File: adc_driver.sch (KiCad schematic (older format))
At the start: 26 parts, among them U17 DG412xUE, U18 AD8421ARZ, U19 ADA4932-1YCPZ-R7

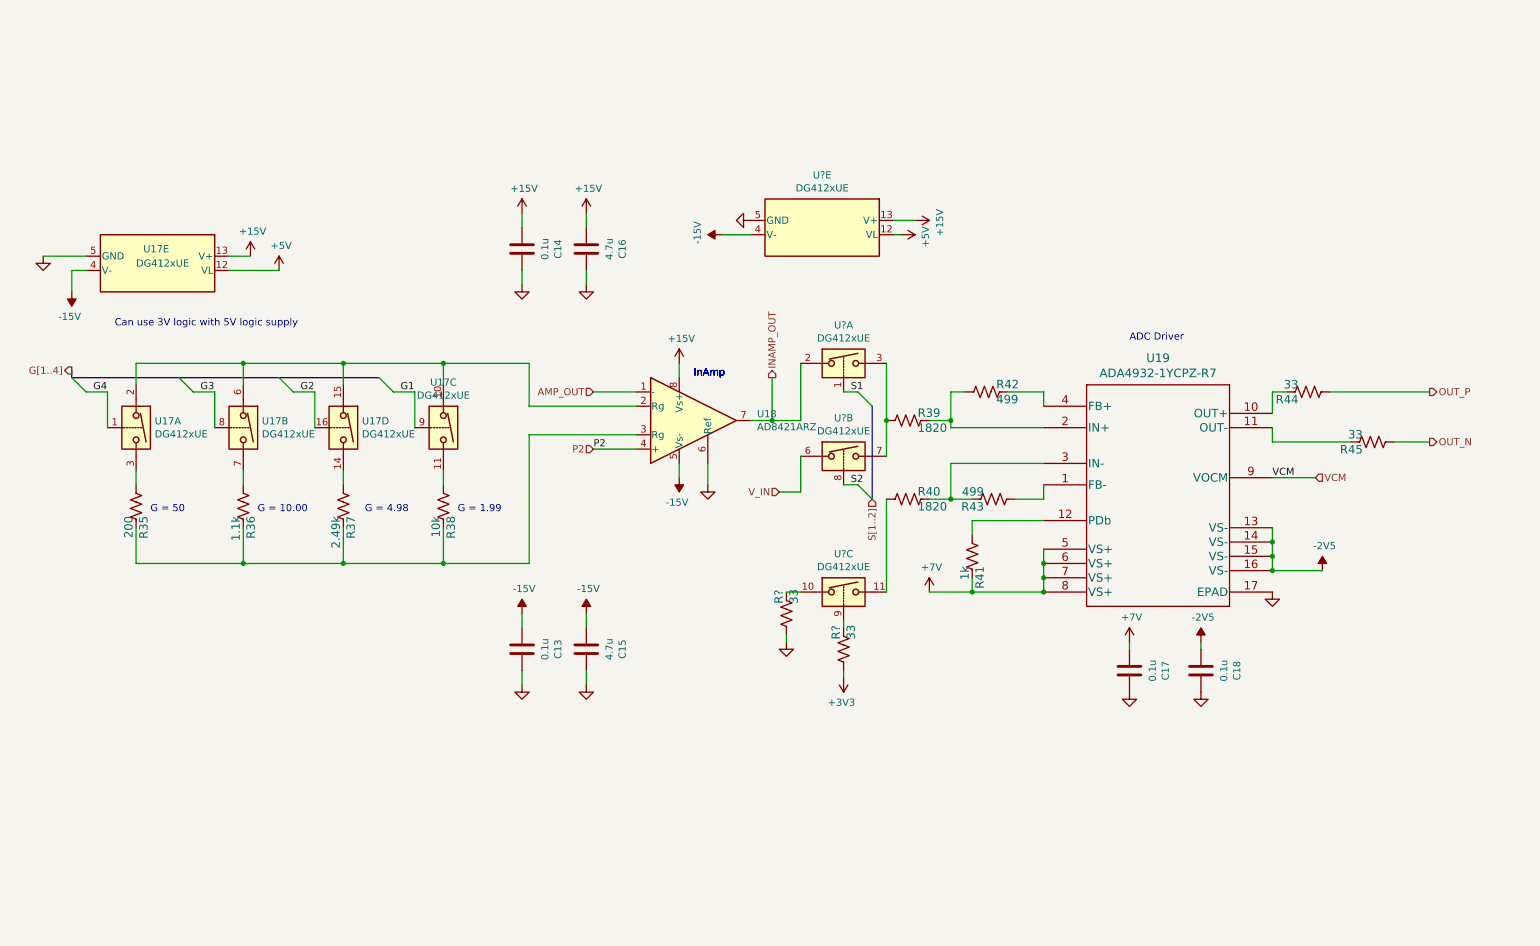
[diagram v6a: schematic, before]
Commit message: update MUX for adc driver
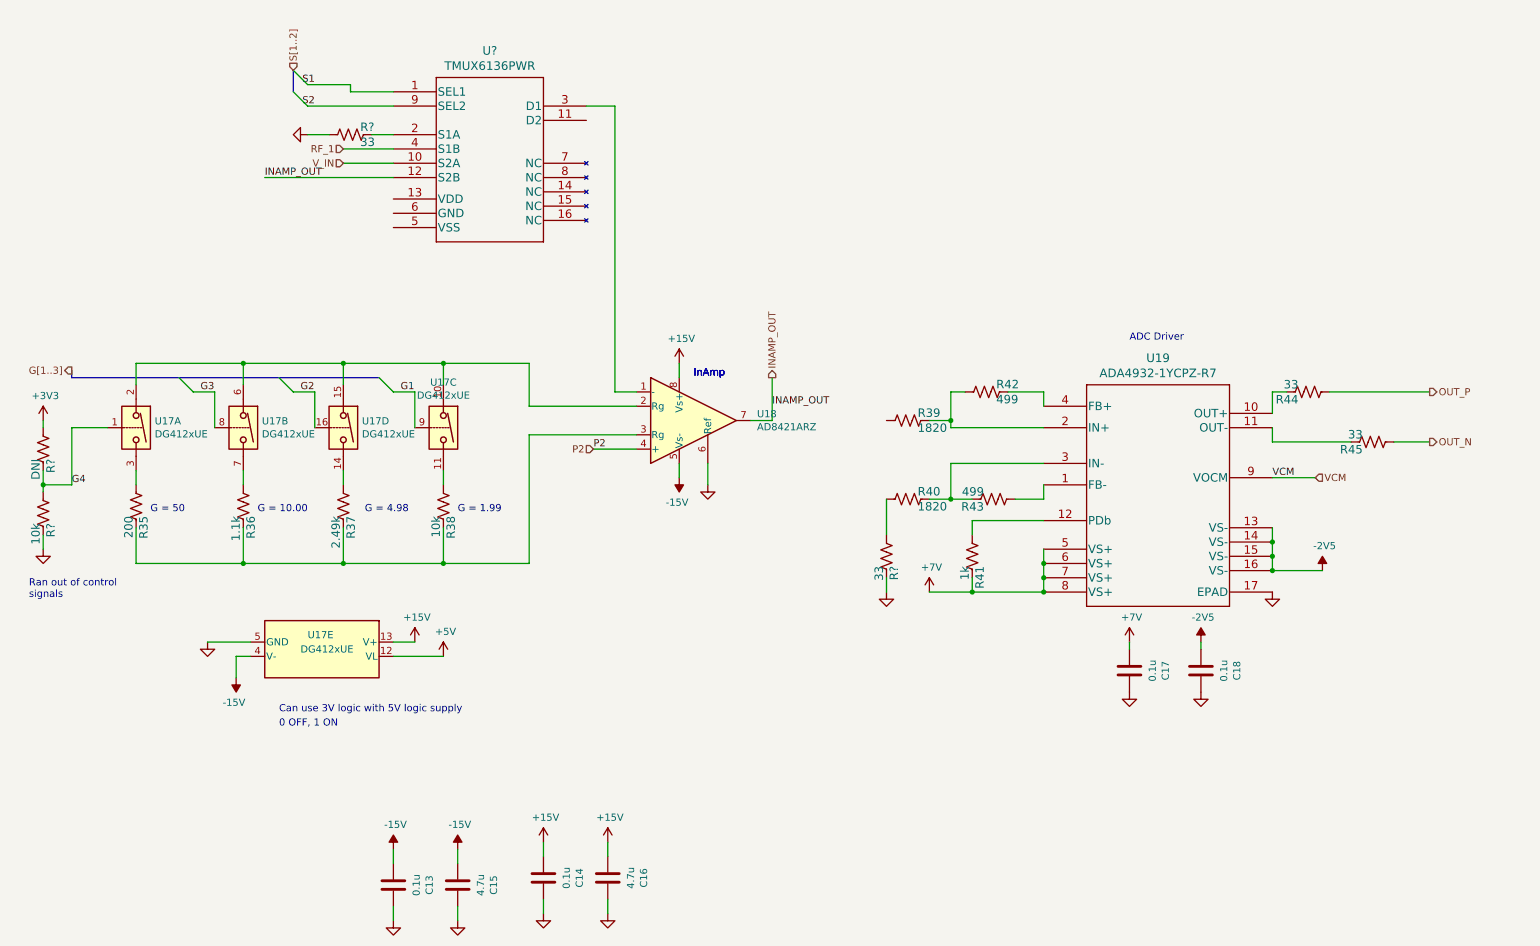
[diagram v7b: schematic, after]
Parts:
- removed R?: 33, Resistor_SMD:R_0603_1608Metric, symbol Device:R_US
- removed U? (x4): DG412xUE, Package_SO:TSSOP-16_4.4x5mm_P0.65mm, symbol Analog_Switch:DG412xUE
- added R?: 33, Resistor_SMD:R_0603_1608Metric, symbol Device:R_US
- added R?: 10k, Resistor_SMD:R_0603_1608Metric, symbol Device:R_US
- added R?: DNI, Resistor_SMD:R_0603_1608Metric, symbol Device:R_US
- added U?: TMUX6136PWR, PW16_TEX, symbol covg-kicad:TMUX6136PWR
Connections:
- net +3V3: now also R?.2
- net G4: now also R?.1, R?.2
- net GND: now also R?.1, R?.1
- net INAMP_OUT: now also U?.12 (S2B)
- net S1: now also U?.1 (SEL1)
- net S2: now also U?.9 (SEL2)
- net V_IN: now also U?.10 (S2A)
- net at R40.2: now also R?.2
- net at R?.1: now also U?.2 (S1A)
- net AMP_OUT: no longer names the net of U18.1 (-)
- net AMP_OUT: now also U?.3 (D1)
- new net RF_1: U?.4 (S1B)
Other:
- note added: "0 OFF, 1 ON"
- note added: "Ran out of control\nsignals\n"
- moved on the sheet: C13, C14, C15, C16, R?, U17E

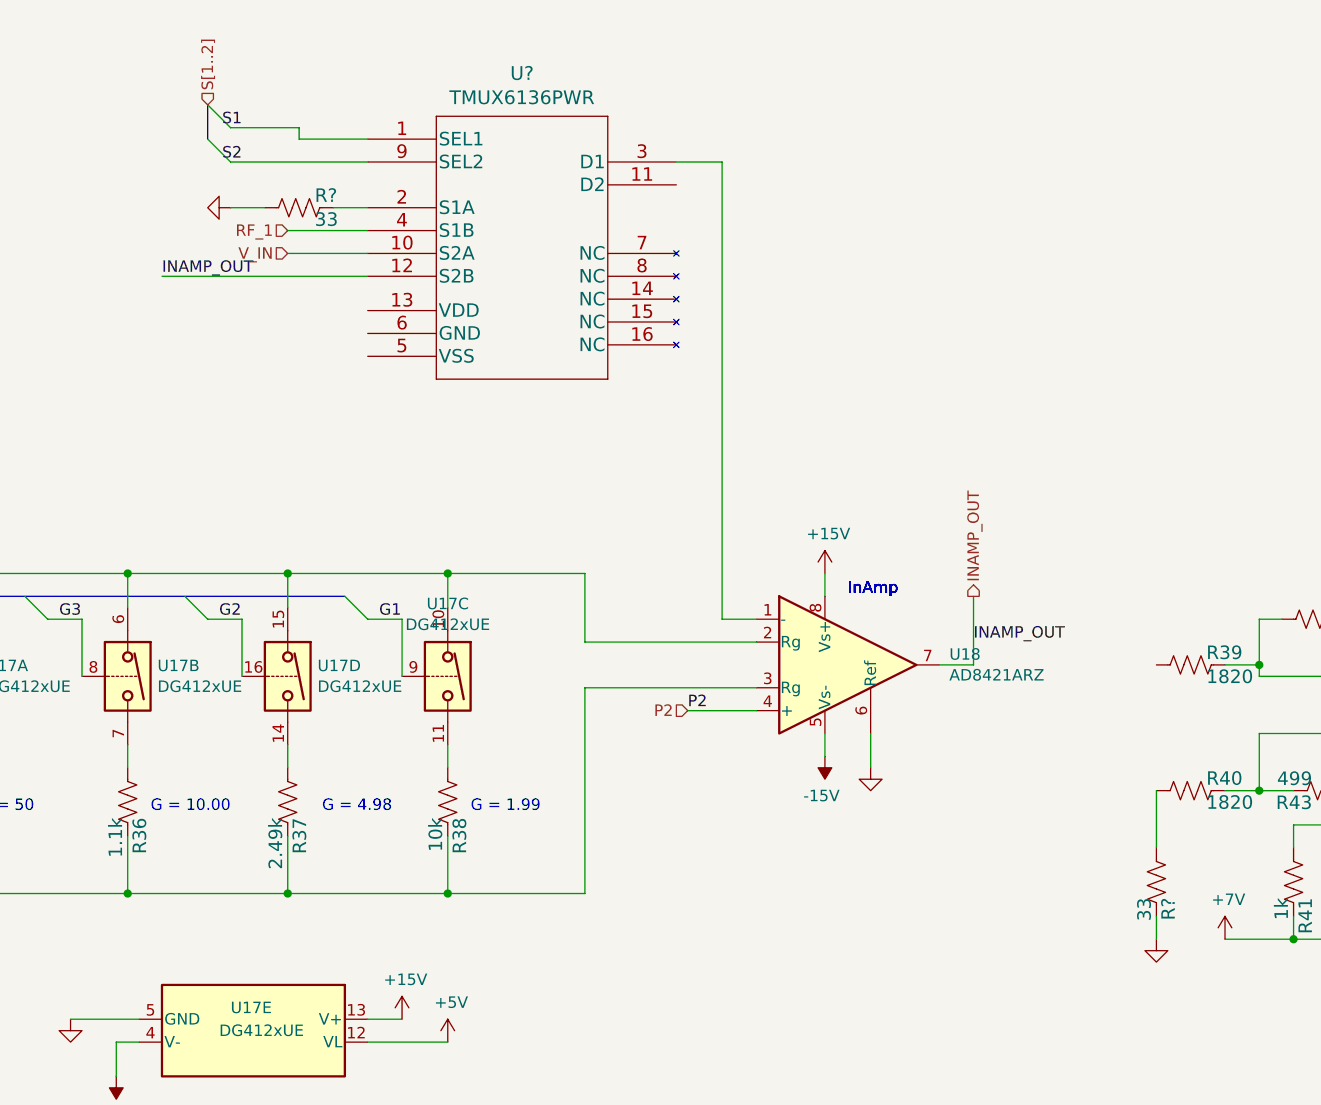
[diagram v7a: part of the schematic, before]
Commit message: added pdf print of schematics
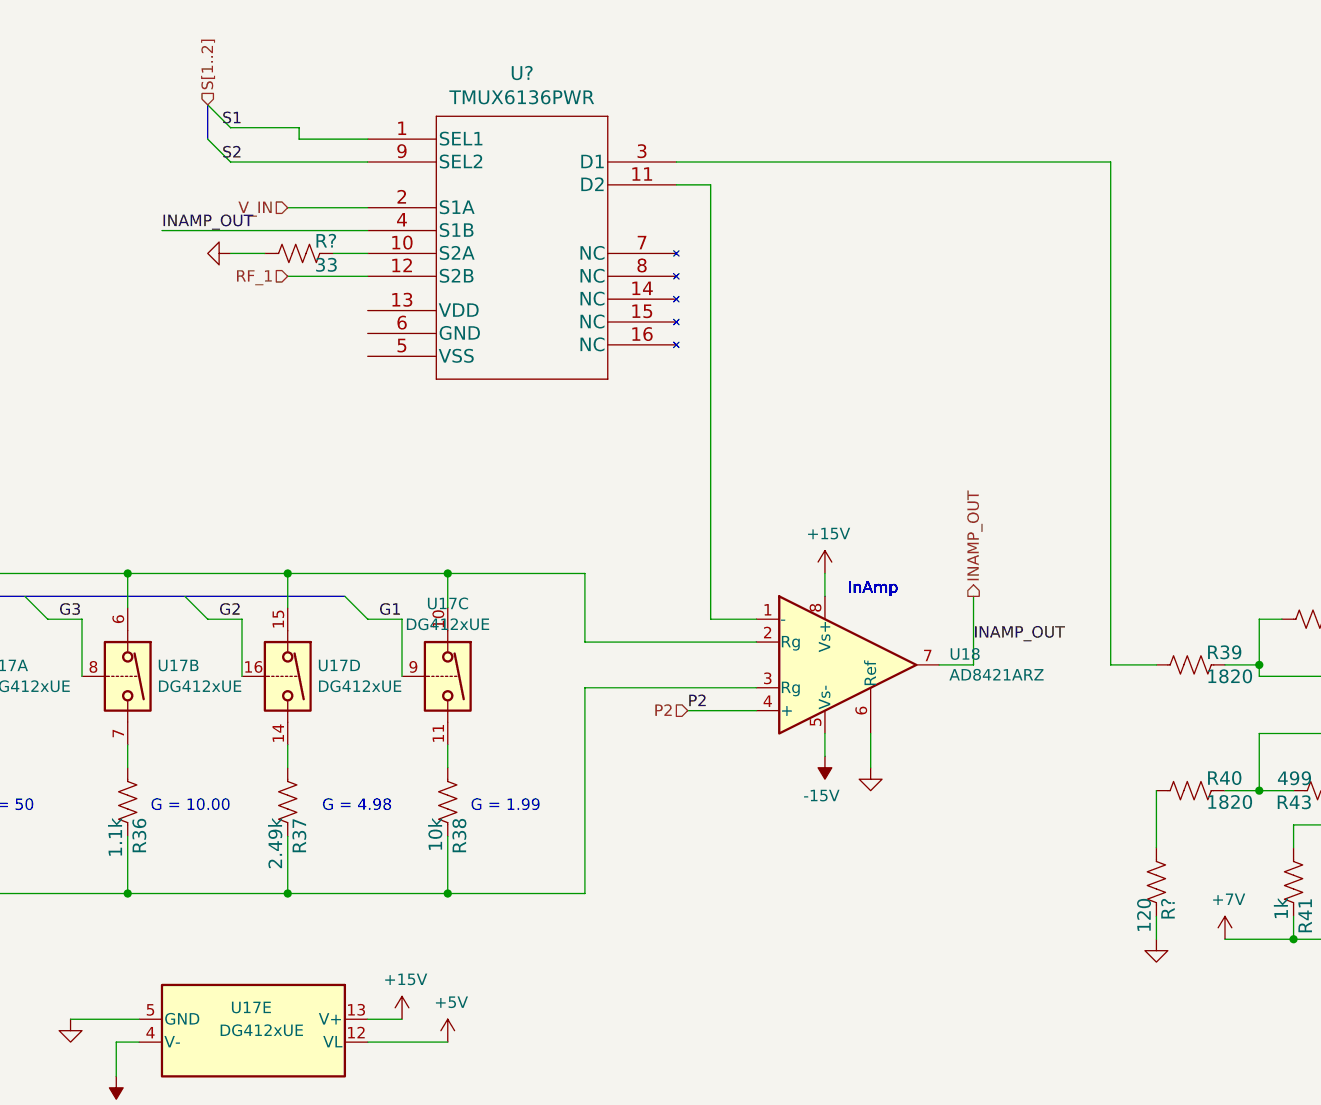
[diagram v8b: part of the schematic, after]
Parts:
- R?: value 33 -> 120; Manf# RC0603FR-0733RL -> RC0603FR-07120RL
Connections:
- net INAMP_OUT: now also U?.4 (S1B); no longer U?.12 (S2B)
- net RF_1: now also U?.12 (S2B); no longer U?.4 (S1B)
- net V_IN: now also U?.2 (S1A); no longer U?.10 (S2A)
- net at R39.2: now also U?.3 (D1)
- net at R?.1: now also U?.10 (S2A); no longer U?.2 (S1A)
- net at U18.1 (-): now also U?.11 (D2); no longer U?.3 (D1)
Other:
- moved on the sheet: R?
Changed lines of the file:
@@
 L power:GND #PWR?
 U 1 1 6097B9AF
-P 2550 1750
+P 2550 1950
 AR Path="/6032F251/6097B9AF" Ref="#PWR?"  Part="1"
 AR Path="/6032F251/608FDC40/6097B9AF" Ref="#PWR063"  Part="1"
-F 0 "#PWR063" H 2550 1500 50  0001 C CNN
-F 1 "GND" V 2555 1622 50  0001 R CNN
-F 2 "" H 2550 1750 50  0001 C CNN
-F 3 "" H 2550 1750 50  0001 C CNN
-	1    2550 1750
+F 0 "#PWR063" H 2550 1700 50  0001 C CNN
+F 1 "GND" V 2555 1822 50  0001 R CNN
+F 2 "" H 2550 1950 50  0001 C CNN
+F 3 "" H 2550 1950 50  0001 C CNN
+	1    2550 1950
 	0    1    1    0
 $EndComp
@@
 Text HLabel 4550 3950 0    50   Input ~ 0
 P2
-Text HLabel 2800 1850 0    50   Input ~ 0
+Text HLabel 2800 2050 0    50   Input ~ 0
 RF_1
 Text HLabel 10400 3550 2    50   Output ~ 0
@@
 L Device:R_US R?
 U 1 1 60B49B76
-P 2850 1750
+P 2850 1950
 AR Path="/6032F251/60B49B76" Ref="R?"  Part="1"
 AR Path="/6032F251/608FDC40/60B49B76" Ref="R?"  Part="1"
-F 0 "R?" V 2797 1818 59  0000 L CNN
-F 1 "33" V 2902 1818 59  0000 L CNN
-F 2 "Resistor_SMD:R_0603_1608Metric" H 2850 1750 50  0001 C CNN
-F 3 "" H 2850 1750 50  0001 C CNN
-F 4 "RC0603FR-0733RL" H 2797 1918 50  0001 C CNN "Manf#"
-F 5 "1%" H 2850 1750 50  0001 C CNN "Tolerance"
-	1    2850 1750
+F 0 "R?" V 2797 2018 59  0000 L CNN
+F 1 "33" V 2902 2018 59  0000 L CNN
+F 2 "Resistor_SMD:R_0603_1608Metric" H 2850 1950 50  0001 C CNN
+F 3 "" H 2850 1950 50  0001 C CNN
+F 4 "RC0603FR-0733RL" H 2797 2118 50  0001 C CNN "Manf#"
+F 5 "1%" H 2850 1950 50  0001 C CNN "Tolerance"
+	1    2850 1950
 	0    1    1    0
 $EndComp
-Text HLabel 2800 1950 0    50   Input ~ 0
+Text HLabel 2800 1750 0    50   Input ~ 0
 V_IN
 Entry Wire Line
@@
 AR Path="/6032F251/608FDC40/62205F18" Ref="R?"  Part="1"
 F 0 "R?" V 6547 4768 59  0000 L CNN
-F 1 "33" V 6652 4768 59  0000 L CNN
+F 1 "120" V 6652 4768 59  0000 L CNN
 F 2 "Resistor_SMD:R_0603_1608Metric" H 6600 4700 50  0001 C CNN
 F 3 "" H 6600 4700 50  0001 C CNN
-F 4 "RC0603FR-0733RL" H 6547 4868 50  0001 C CNN "Manf#"
+F 4 "RC0603FR-07120RL" H 6547 4868 50  0001 C CNN "Manf#"
 F 5 "1%" H 6600 4700 50  0001 C CNN "Tolerance"
 	1    6600 4700
@@
 	6600 4550 6600 4300
 Wire Wire Line
-	2800 1850 3150 1850
-Wire Wire Line
-	4700 1550 4700 3550
-Wire Wire Line
-	4700 3550 4850 3550
+	2800 2050 3150 2050
 Text Notes 2350 5900 0    50   ~ 0
 0 OFF, 1 ON
@@
 Ran out of control\nsignals\n
 Wire Wire Line
-	2550 1750 2700 1750
-Wire Wire Line
-	3000 1750 3150 1750
+	2550 1950 2700 1950
+Wire Wire Line
+	3000 1950 3150 1950
 $Comp
 L covg-kicad:TMUX6136PWR U?
@@
 $EndComp
 Wire Wire Line
-	4500 1550 4700 1550
-Wire Wire Line
 	2850 1400 2850 1450
 Wire Wire Line
@@
 INAMP_OUT
 Wire Wire Line
-	3150 2050 2250 2050
-Wire Wire Line
-	2800 1950 3150 1950
-Text Label 2250 2050 0    50   ~ 0
+	3150 1850 2250 1850
+Wire Wire Line
+	2800 1750 3150 1750
+Text Label 2250 1850 0    50   ~ 0
 INAMP_OUT
+Wire Wire Line
+	4500 1650 4650 1650
+Wire Wire Line
+	4650 1650 4650 3550
+Wire Wire Line
+	4650 3550 4850 3550
+Wire Wire Line
+	4500 1550 6400 1550
+Wire Wire Line
+	6400 1550 6400 3750
+Wire Wire Line
+	6400 3750 6600 3750
 Wire Bus Line
 	900  3450 3050 3450
